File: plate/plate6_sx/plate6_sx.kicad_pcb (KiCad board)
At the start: 2 copper layers, 157.5 x 113.2 mm, 0 parts

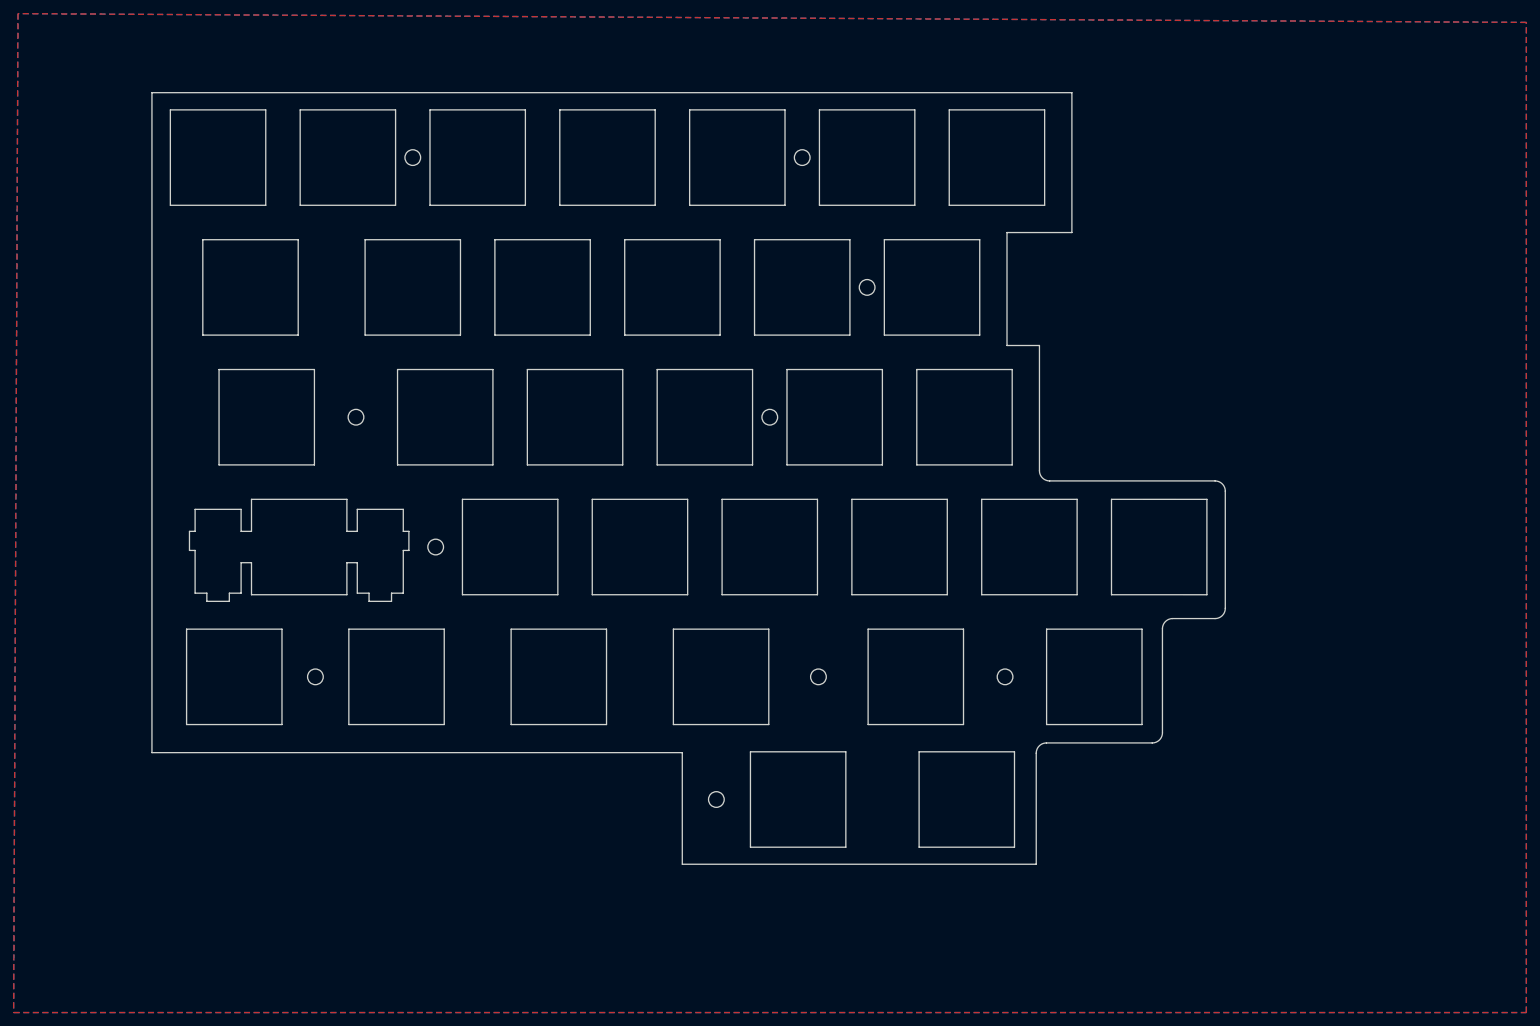
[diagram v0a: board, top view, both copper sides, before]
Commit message: tastiera con rj11 mandata in stampa
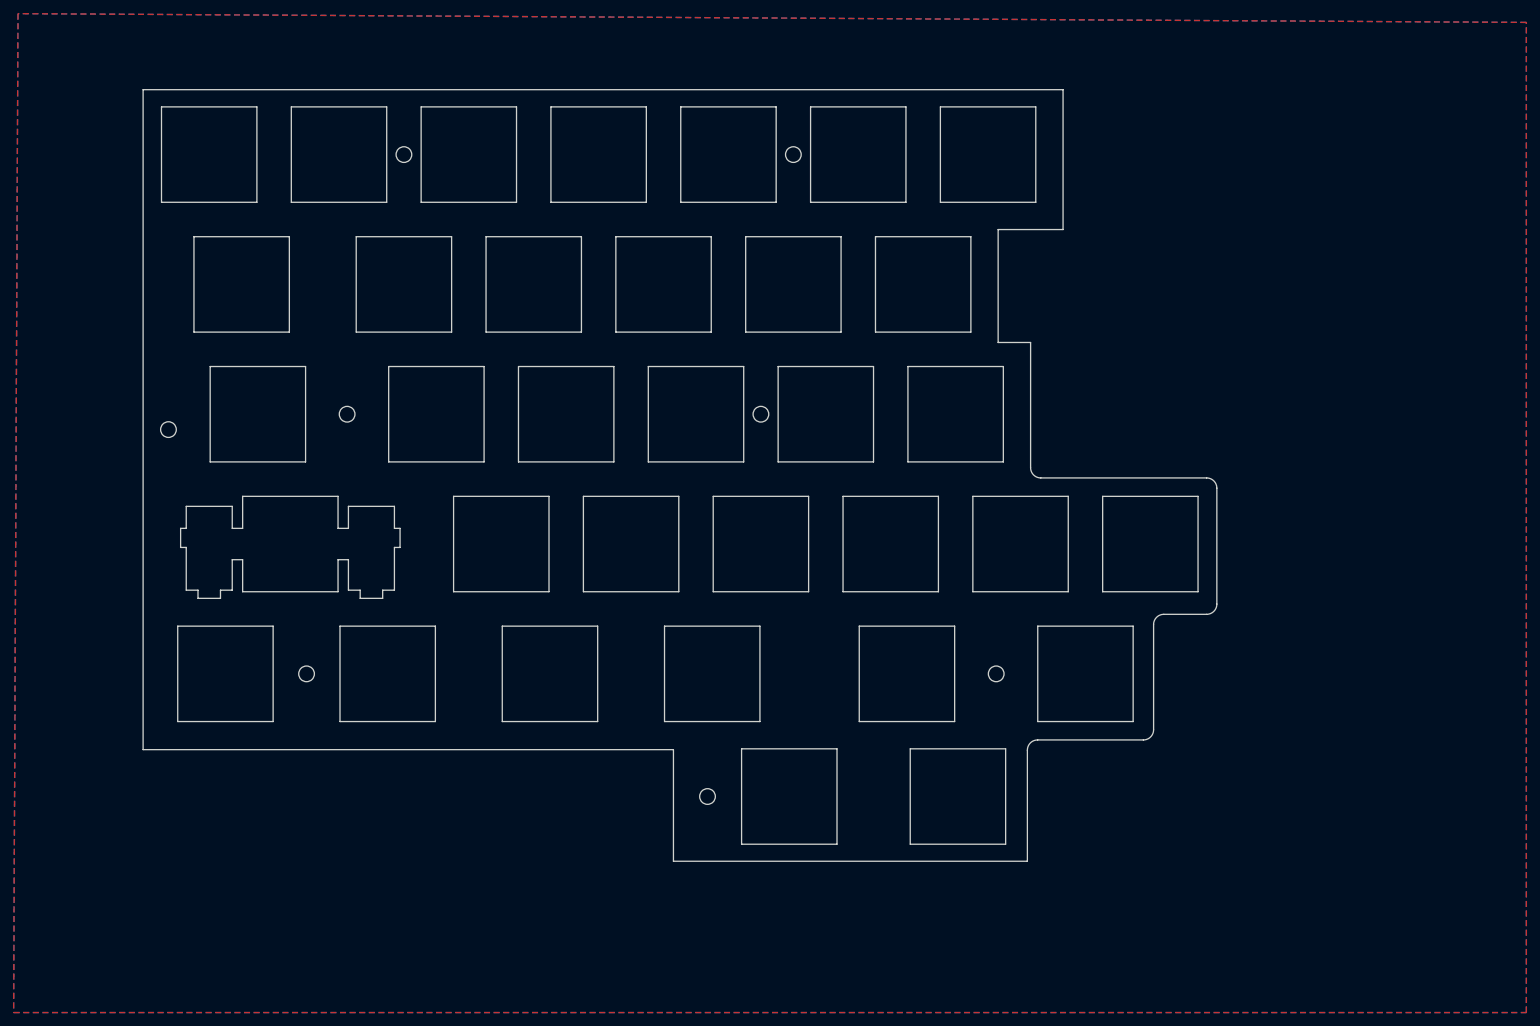
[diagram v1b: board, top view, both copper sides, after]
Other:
- board size 157.5 x 113.2 mm -> 157.6 x 113.2 mm
